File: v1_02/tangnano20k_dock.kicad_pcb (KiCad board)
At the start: 2 copper layers, 161.9 x 73.7 mm, 105 parts, among them J1 Mini-DIN-6, J10 DB9_Male_MountingHoles, J11 DA15_Socket_MountingHoles, J12 Cliff DC10A, J13 Aliexpress ADS1115 module, J14 Mini-DIN-6, J15 Conn_01x01_Pin, J17 Conn_01x03_Pin, J18 Conn_02x04_Odd_Even, J2 2x20 Pin Female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

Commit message: v1_02: Updated symbols/footprints for KiCAD9; fix all ERC/DRC warnings
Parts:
- BT1: value CR2020 -> CR20xx
- J3: value Conn_01x03_Male -> Conn_01x03_Pin
- L1, L2, L3, L4, L5, L6: footprint Inductor_SMD:L_1206_3216Metric_Pad1.42x1.75mm_HandSolder -> Inductor_SMD:L_1206_3216Metric_Pad1.22x1.90mm_HandSolder
- R26: value R -> 15K
- R27, R28: value R -> 3K3
- Y1: footprint Crystal:Crystal_SMD_3215-2Pin_3.2x1.5mm -> TangNano20k:Crystal_SMD_3215-2Pin_3.2x1.5mm
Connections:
- net /Joysticks/<NO NET> renamed /Joysticks/AGND
- net PWM_L renamed /PWM_L
- net PWM_R renamed /PWM_R
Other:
- board text added: "BeebFPGA Dock for the Tang Nano 20K Version 1.02 (c) 2025 Hoglet"
- board text removed: "BeebFPGA Dock for the Tang Nano 20K Version 1.01 (c) 2025 Hoglet"

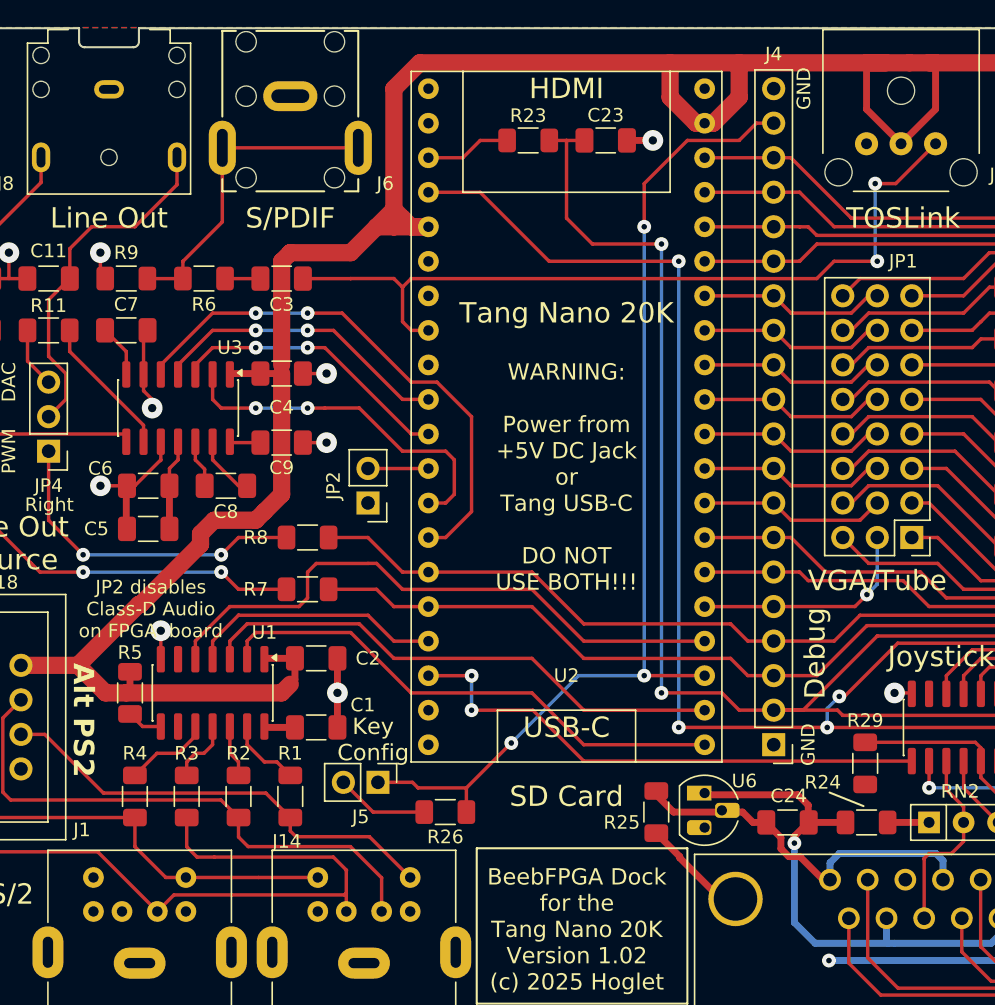
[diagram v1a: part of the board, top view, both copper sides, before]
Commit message: v1_02: Increase PS/2 + Tang hole sizes; corrected U6 symbol
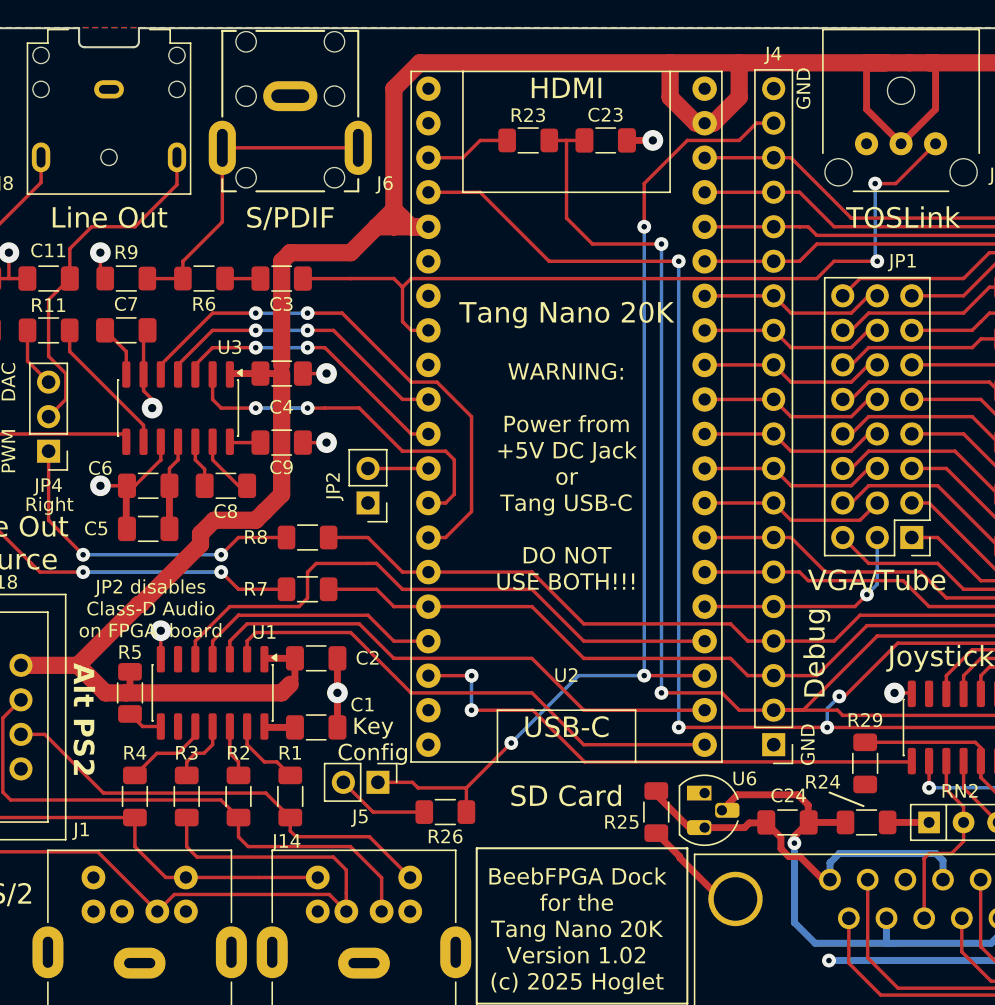
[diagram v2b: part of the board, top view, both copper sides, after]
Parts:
- J10: value DB9_Male_MountingHoles -> DE9_Pins_MountingHoles
- U6: footprint Package_TO_SOT_THT:TO-92L_HandSolder -> Package_TO_SOT_THT:TO-92_HandSolder
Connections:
- U6 pad 1: /Joysticks/VREF -> (no net)
- U6 pad 2: /Joysticks/AGND -> /Joysticks/VREF
- U6 pad 3: unconnected-(U6-NC-Pad3) -> /Joysticks/AGND
